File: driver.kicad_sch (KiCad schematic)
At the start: 7 parts, among them U10 74AUC2G32, U11 SN74AUP2G08, U12 74AUC2G32, U6 Inverter_Schmitt_Dual, U7 Inverter_Schmitt_Dual, U8 SN74AUP2G08, U9 74AUC2G32

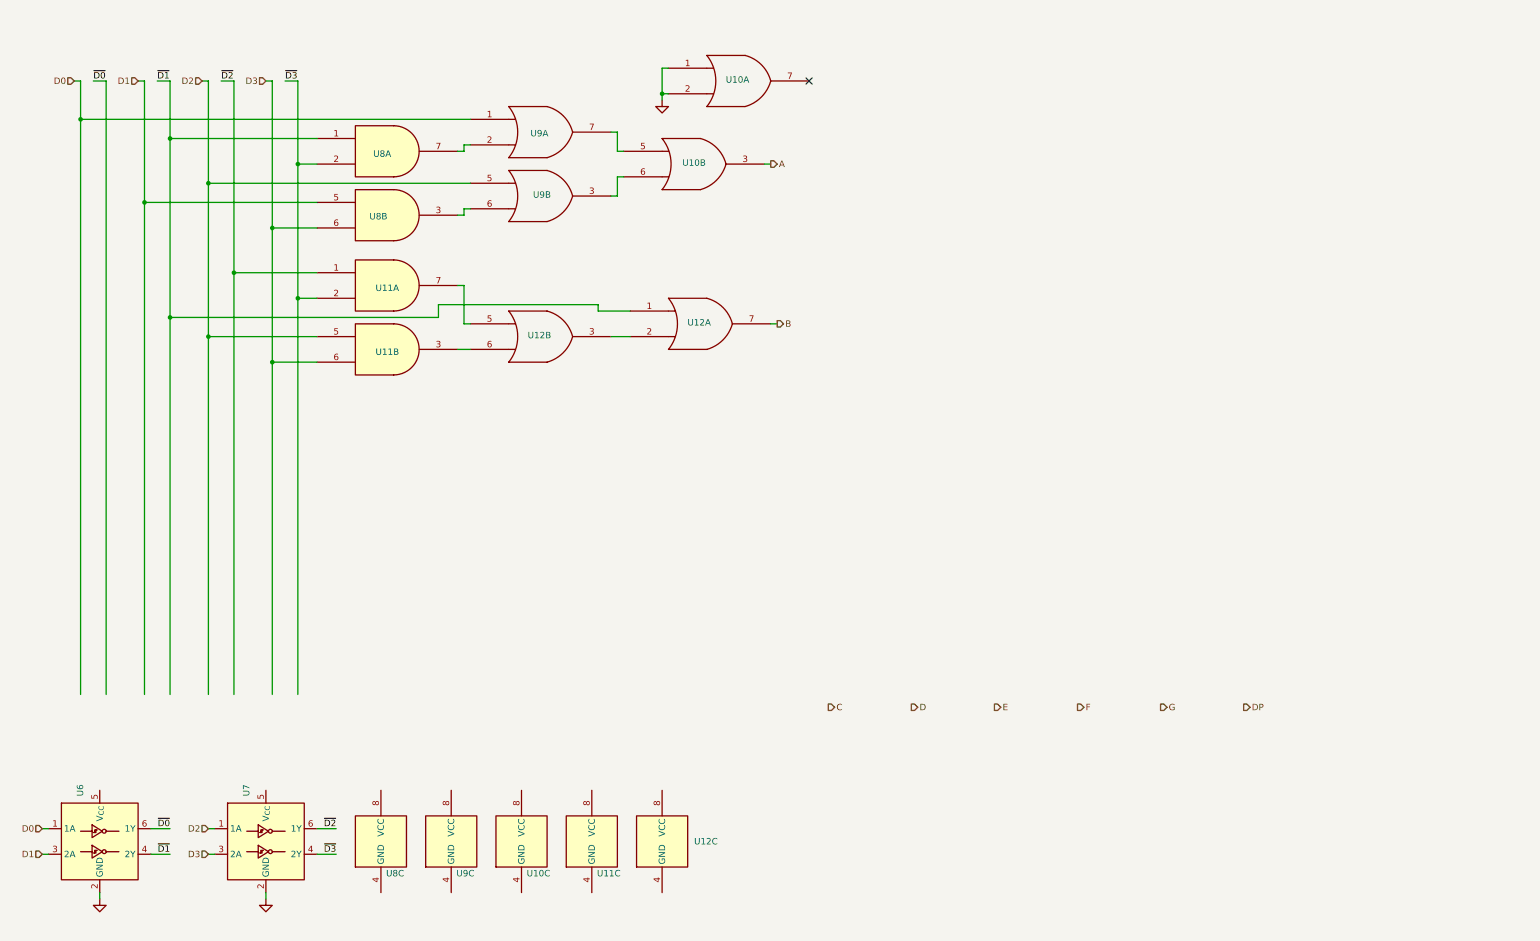
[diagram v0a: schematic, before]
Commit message: schem: add c segment driver
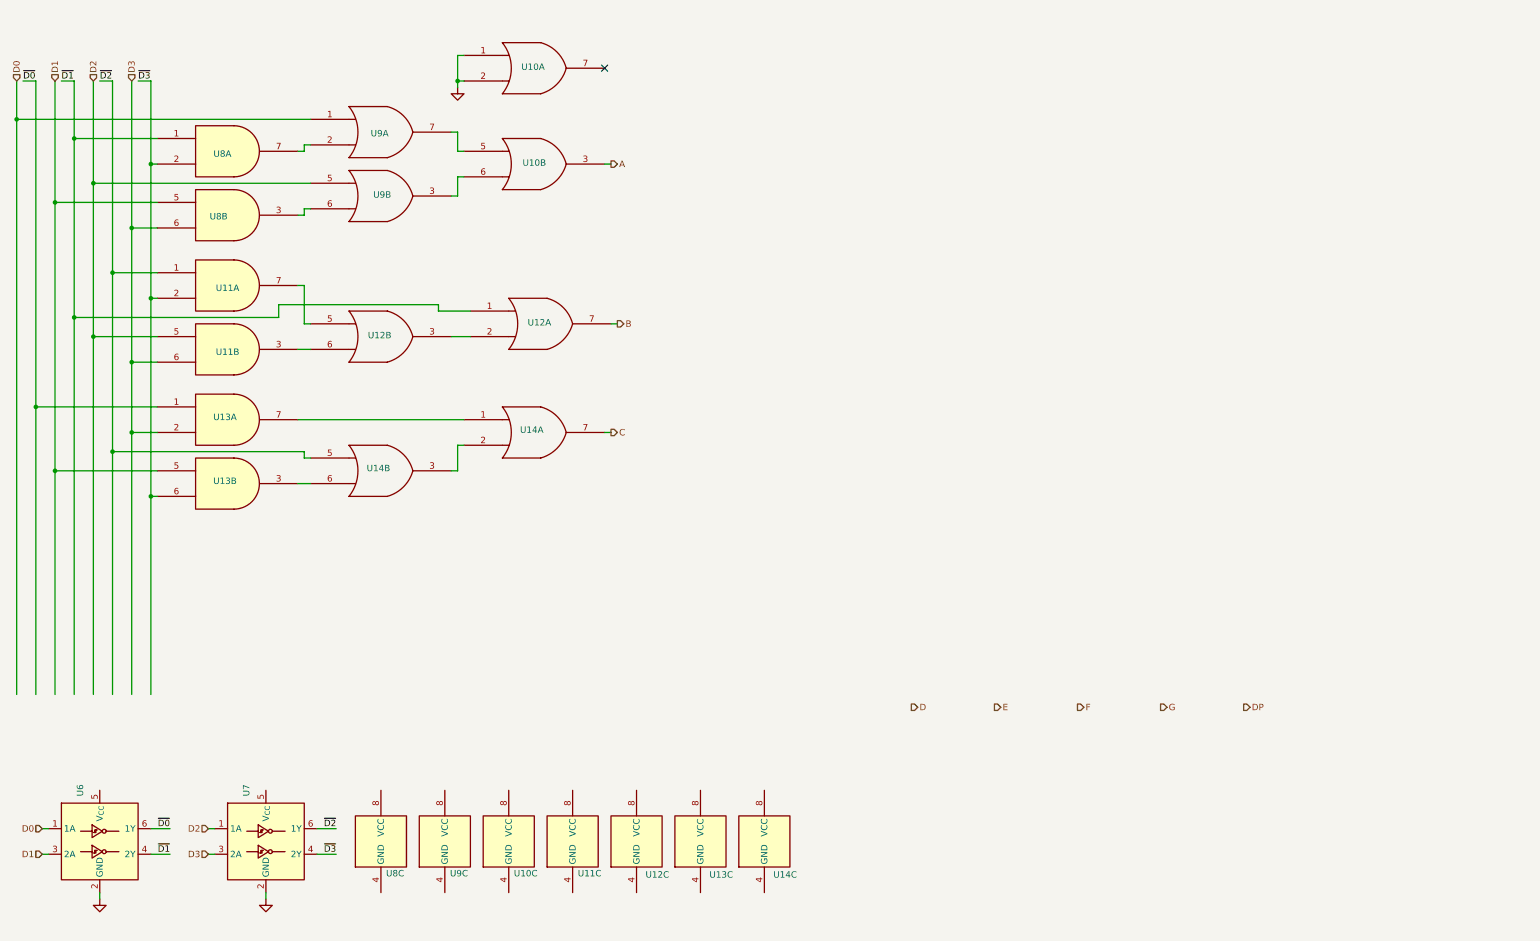
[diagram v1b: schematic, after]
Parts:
- added U13: SN74AUP2G08, Package_SO:VSSOP-8_2.3x2mm_P0.5mm, symbol GLCS:SN74AUP2G08
- added U14: 74AUC2G32, Package_DFN_QFN:QFN-20-1EP_5x5mm_P0.65mm_EP3.35x3.35mm, symbol 74xGxx:74AUC2G32
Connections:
- net C: now also U14.7
- net D1: now also U13.5
- net D3: now also U13.2
- net ~{D0}: now also U13.1
- net ~{D2}: now also U14.5
- net ~{D3}: now also U13.6
- new net: U13.7, U14.1
- new net: U14.2, U14.3
- new net: U13.3, U14.6
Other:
- moved on the sheet: U10A, U10B, U10C, U11A, U11B, U11C, U12A, U12B, U12C, U8A, U8B, U9A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

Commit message: schem: add d segment
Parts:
- added U15, U16, U17: SN74AUP2G08, Package_SO:VSSOP-8_2.3x2mm_P0.5mm, symbol GLCS:SN74AUP2G08
- added U18, U19: 74AUC2G32, Package_DFN_QFN:QFN-20-1EP_5x5mm_P0.65mm_EP3.35x3.35mm, symbol 74xGxx:74AUC2G32
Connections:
- net D: now also U18.7
- net D1: now also U17.1
- net D2: now also U15.6, U16.5
- net D3: now also U16.2
- net GND: now also U17.5, U17.6, U19.1, U19.2
- net ~{D1}: now also U15.1, U15.5
- net ~{D2}: now also U16.1
- net ~{D3}: now also U15.2, U16.6
- new net: U18.1, U19.3
- new net: U15.7, U19.5
- new net: U15.3, U19.6
- new net: U18.2, U18.3
- new net: U16.7, U17.2
- new net: U16.3, U18.6
- new net: U17.7, U18.5
- no-connect marks 1 -> 3
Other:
- moved on the sheet: U10A

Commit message: schem: add ef segments
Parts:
- added U20, U22, U24: SN74AUP2G08, Package_SO:VSSOP-8_2.3x2mm_P0.5mm, symbol GLCS:SN74AUP2G08
- added U21, U23, U25: 74AUC2G32, Package_DFN_QFN:QFN-20-1EP_5x5mm_P0.65mm_EP3.35x3.35mm, symbol 74xGxx:74AUC2G32
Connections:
- net D0: now also U23.5
- net D1: now also U22.1, U24.1
- net D2: now also U20.5
- net E: now also U21.3
- net F: now also U25.3
- net GND: now also U21.1, U21.2, U22.5, U22.6, U23.1, U23.2
- net ~{D1}: now also U20.1
- net ~{D2}: now also U22.2, U24.5
- net ~{D3}: now also U20.2, U20.6, U24.2, U24.6
- new net: U20.7, U21.5
- new net: U20.3, U21.6
- new net: U22.7, U23.6
- new net: U24.3, U25.2
- new net: U24.7, U25.1
- new net: U25.6, U25.7
- new net: U23.3, U25.5
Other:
- moved on the sheet: U15C, U16C, U17C, U18C, U19A, U19C

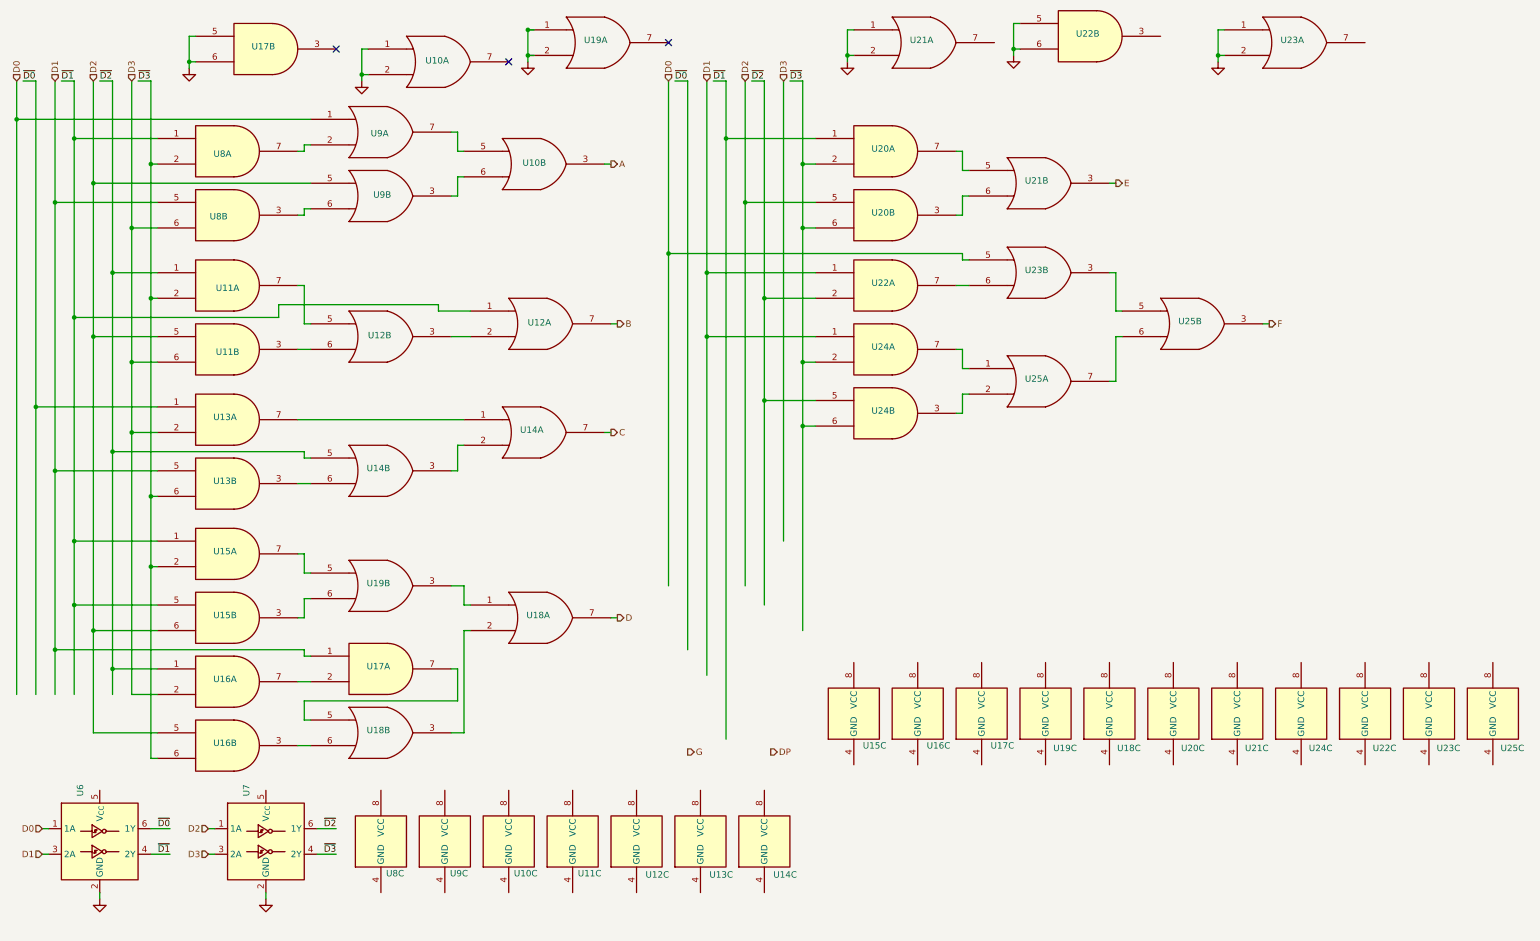
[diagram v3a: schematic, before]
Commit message: schem: add decoupling gates caps
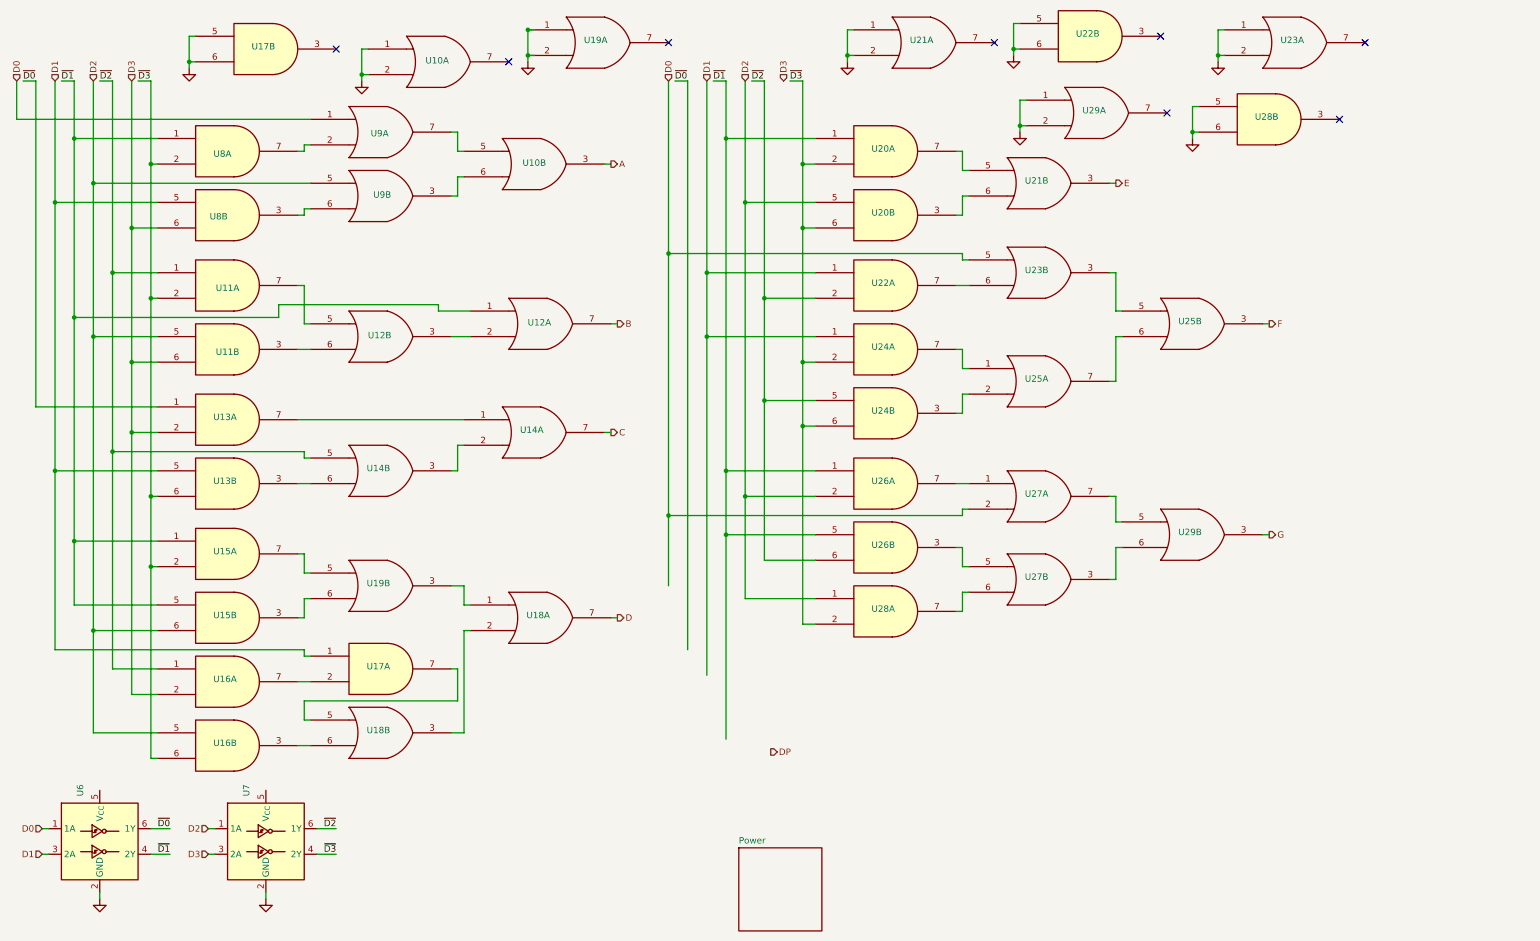
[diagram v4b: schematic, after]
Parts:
- removed unit 3 of U10
- removed unit 3 of U11
- removed unit 3 of U12
- removed unit 3 of U13
- removed unit 3 of U14
- removed unit 3 of U15
- removed unit 3 of U16
- removed unit 3 of U17
- removed unit 3 of U18
- removed unit 3 of U19
- removed unit 3 of U20
- removed unit 3 of U21
- removed unit 3 of U22
- removed unit 3 of U23
- removed unit 3 of U24
- removed unit 3 of U25
- removed unit 3 of U8
- removed unit 3 of U9
- added U26, U28: SN74AUP2G08, Package_SO:VSSOP-8_2.3x2mm_P0.5mm, symbol GLCS:SN74AUP2G08
- added U27, U29: 74AUC2G32, Package_DFN_QFN:QFN-20-1EP_5x5mm_P0.65mm_EP3.35x3.35mm, symbol 74xGxx:74AUC2G32
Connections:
- net D0: now also U27.2
- net D2: now also U26.2, U28.1
- net G: now also U29.3
- net GND: now also U28.5, U28.6, U29.1, U29.2
- net ~{D1}: now also U26.1, U26.5
- net ~{D2}: now also U26.6
- net ~{D3}: now also U28.2
- new net: U26.7, U27.1
- new net: U27.7, U29.5
- new net: U27.3, U29.6
- new net: U26.3, U27.5
- new net: U27.6, U28.7
- no-connect marks 3 -> 8
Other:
- added sheet Power (power.kicad_sch)
